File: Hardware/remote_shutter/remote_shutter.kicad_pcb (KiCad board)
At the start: 4 copper layers, 78 x 57 mm, 62 parts, among them J1 USB_C_Receptacle_USB2.0, J2 OLED, J3 AudioJack3, J4 Buzzer, J6 Switch, Q1 DMN2056U, Q2 DMN2056U, Q3 BC847BDW1, SW1 RotaryEncoder_Switch, U1 AZ1117-3.3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

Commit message: DRC error fixes.
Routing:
- net Net-(Q3-Pad5): track 0.00 -> 4.95 mm, vias 0 -> 1
- net GND: track 160.9 -> 165.3 mm, vias 26 -> 27
- net /DP: track 5.19 -> 8.74 mm, vias 0 -> 2
- net /DN: track 5.19 -> 7.92 mm
- net +3V3: track 38.0 -> 39.6 mm
- net /MCU/Interfaces/I2C.SCL: track 60.6 -> 59.9 mm

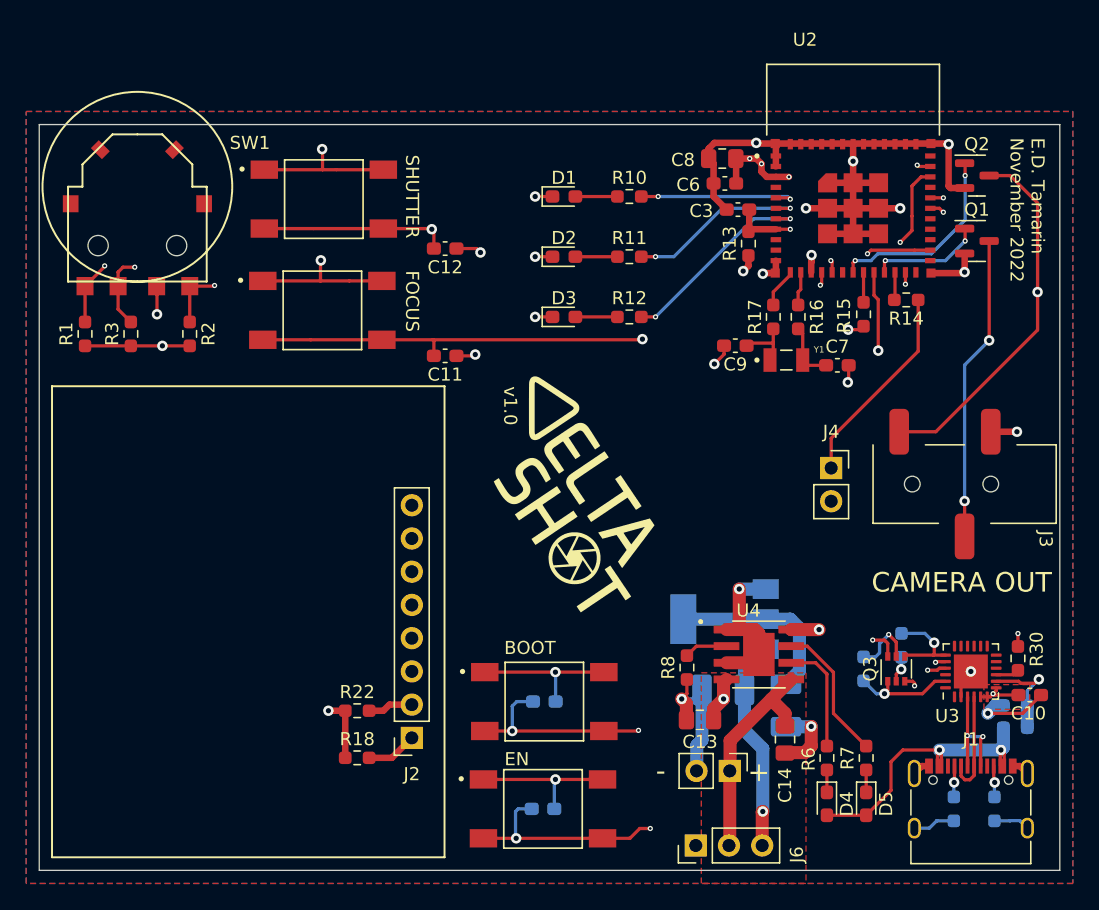
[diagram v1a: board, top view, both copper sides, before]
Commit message: Fixed via sizes. Added IO0 pullup.
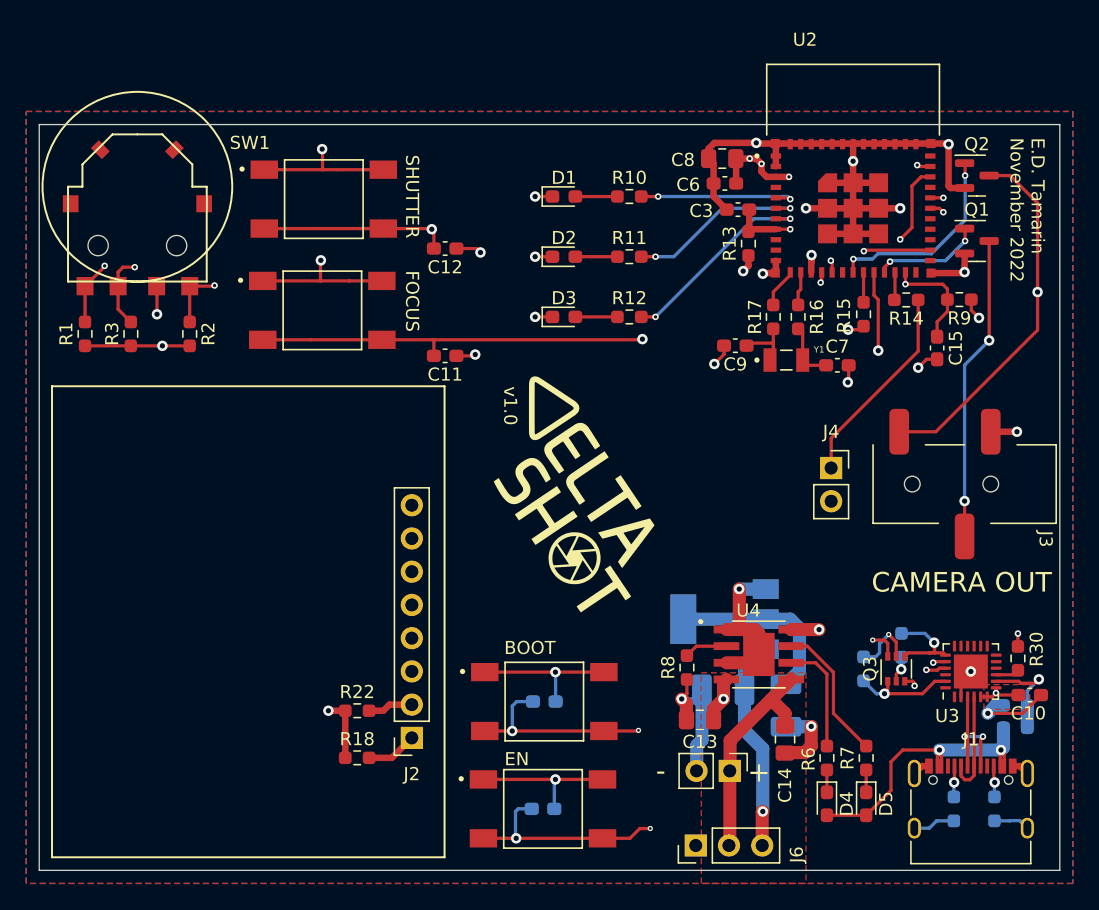
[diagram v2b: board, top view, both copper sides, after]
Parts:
- added C15: 0u1, Capacitor_SMD:C_0603_1608Metric_Pad1.08x0.95mm_HandSolder, F.Cu at (173.1, 86.1)
- added R9: 10k, Resistor_SMD:R_0603_1608Metric_Pad0.98x0.95mm_HandSolder, F.Cu at (174.8, 82.4)
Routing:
- net /MCU/IO0: track 67.9 -> 75.2 mm
- net /MCU/Interfaces/I2C.SCL: track 59.9 -> 58.0 mm
- net GND: track 165.3 -> 167.0 mm, vias 27 -> 28
- net +3V3: track 39.6 -> 41.1 mm, vias 8 -> 9

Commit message: Added debug connectors
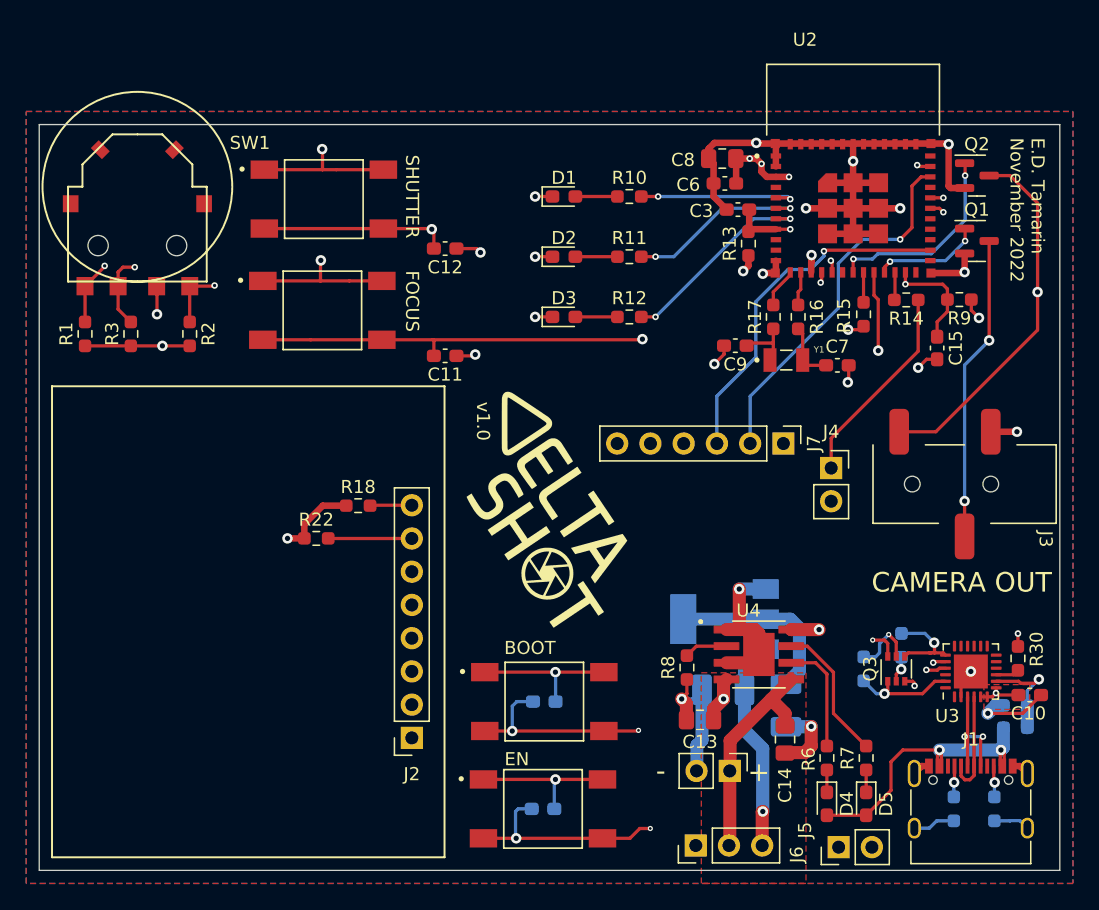
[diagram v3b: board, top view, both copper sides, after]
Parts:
- added J5: Conn_01x02_Male, Connector_PinHeader_2.54mm:PinHeader_1x02_P2.54mm_Vertical, F.Cu at (165.6, 124.2)
- added J7: Conn_01x06_Male, Connector_PinHeader_2.54mm:PinHeader_1x06_P2.54mm_Vertical, F.Cu at (161.3, 93.4)
- moved R18 19.3 mm to (128.8, 98.2)
- moved R22 13.5 mm to (125.7, 100.7)
- moved G*** 2.39 mm to (143.4, 99.2)
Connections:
- net /Comms/RX renamed /MCU/TX
- net /Comms/TX renamed /MCU/RX
- J2 pad 1: /MCU/Interfaces/I2C.SDA -> GND
- J2 pad 2: /MCU/Interfaces/I2C.SCL -> /MCU/Interfaces/5V
- J2 pad 3: /MCU/Interfaces/D/C -> +3V3
- J2 pad 4: /MCU/RST -> /MCU/Interfaces/CS
- J2 pad 5: /MCU/Interfaces/CS -> /MCU/RST
- J2 pad 6: +3V3 -> /MCU/Interfaces/D/C
- J2 pad 7: /MCU/Interfaces/5V -> /MCU/Interfaces/I2C.SCL
- J2 pad 8: GND -> /MCU/Interfaces/I2C.SDA
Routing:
- net /MCU/EN: track 93.5 -> 22.5 mm
- net /MCU/Interfaces/A2: track 61.5 -> 6.79 mm
- net /MCU/IO0: track 75.2 -> 26.0 mm
- net /MCU/Interfaces/A1: track 52.9 -> 5.47 mm
- net /MCU/RST: track 51.9 -> 7.91 mm
- net /MCU/TX: track 38.3 -> 31.2 mm
- net /MCU/RX: track 38.3 -> 33.3 mm
- net /MCU/Interfaces/I2C.SDA: track 65.4 -> 61.4 mm
- net /MCU/Interfaces/I2C.SCL: track 58.0 -> 61.8 mm
- net +3V3: track 41.1 -> 42.4 mm
- net /MCU/Interfaces/5V: track 0.00 -> 0.76 mm

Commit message: Updated routing, ground plane now empty
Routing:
- net /MCU/RST: track 7.91 -> 59.0 mm
- net /MCU/EN: track 22.5 -> 60.3 mm
- net /MCU/TX: track 31.2 -> 66.4 mm, vias 2 -> 3
- net /MCU/RX: track 33.3 -> 67.7 mm, vias 2 -> 3
- net /MCU/IO0: track 26.0 -> 54.1 mm
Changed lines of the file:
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@@
   (via (at 171.3775 111.9225) (size 0.5) (drill 0.25) (layers "F.Cu" "B.Cu") (net 3))
   (via (at 151.1775 122.8225) (size 0.4) (drill 0.2) (layers "F.Cu" "B.Cu") (net 3))
+  (segment (start 170.603235 111.9225) (end 164.730735 106.05) (width 0.25) (layer "In1.Cu") (net 3))
+  (segment (start 171.3775 111.9225) (end 170.603235 111.9225) (width 0.25) (layer "In1.Cu") (net 3))
+  (segment (start 151.1775 108.758218) (end 151.1775 122.8225) (width 0.25) (layer "In1.Cu") (net 3))
+  (segment (start 153.885718 106.05) (end 151.1775 108.758218) (width 0.25) (layer "In1.Cu") (net 3))
+  (segment (start 164.730735 106.05) (end 153.885718 106.05) (width 0.25) (layer "In1.Cu") (net 3))
   (segment (start 140.8775 123.5225) (end 140.9275 123.5725) (width 0.25) (layer "B.Cu") (net 3))
   (segment (start 140.8775 121.5225) (end 140.8775 123.5225) (width 0.25) (layer "B.Cu") (net 3))
@@
   (via (at 170.6775 81.2225) (size 0.5) (drill 0.25) (layers "F.Cu" "B.Cu") (net 4))
   (via (at 140.6275 115.3725) (size 0.8) (drill 0.4) (layers "F.Cu" "B.Cu") (net 4))
+  (segment (start 153.85 105.45) (end 150.2775 109.0225) (width 0.25) (layer "In1.Cu") (net 4))
+  (segment (start 150.2775 109.0225) (end 150.2775 115.3225) (width 0.25) (layer "In1.Cu") (net 4))
+  (segment (start 168.1775 108.4225) (end 168.1775 106.4775) (width 0.25) (layer "In1.Cu") (net 4))
+  (segment (start 167.15 105.45) (end 153.85 105.45) (width 0.25) (layer "In1.Cu") (net 4))
+  (segment (start 168.1775 106.4775) (end 167.15 105.45) (width 0.25) (layer "In1.Cu") (net 4))
   (segment (start 170.5775 83.2225) (end 170.6775 83.1225) (width 0.25) (layer "In2.Cu") (net 4))
   (segment (start 140.9775 113.1225) (end 140.6275 113.4725) (width 0.25) (layer "B.Cu") (net 4))
@@
   (segment (start 168.2775 80.3225) (end 168.2775 82.0775) (width 0.25) (layer "F.Cu") (net 11))
   (via (at 168.6 86.3) (size 0.8) (drill 0.4) (layers "F.Cu" "B.Cu") (net 11))
+  (segment (start 130.95 103.735) (end 130.95 96.7) (width 0.25) (layer "In1.Cu") (net 11))
+  (segment (start 138.202989 89.447011) (end 167.252989 89.447011) (width 0.25) (layer "In1.Cu") (net 11))
+  (segment (start 167.252989 89.447011) (end 168.6 88.1) (width 0.25) (layer "In1.Cu") (net 11))
+  (segment (start 132.9525 105.7375) (end 130.95 103.735) (width 0.25) (layer "In1.Cu") (net 11))
   (segment (start 168.6 86.3) (end 168.6 88.1) (width 0.25) (layer "In1.Cu") (net 11))
+  (segment (start 130.95 96.7) (end 138.202989 89.447011) (width 0.25) (layer "In1.Cu") (net 11))
   (segment (start 133.717482 113.3575) (end 132.9525 113.3575) (width 0.25) (layer "In2.Cu") (net 13))
   (segment (start 165.0025 92.9975) (end 165.0025 95.2725) (width 0.25) (layer "F.Cu") (net 14))
@@
   (segment (start 177.615 111.0725) (end 178.94 111.0725) (width 0.25) (layer "F.Cu") (net 33))
   (segment (start 172.296964 110.722511) (end 173.119261 110.722511) (width 0.25) (layer "F.Cu") (net 36))
+  (segment (start 151.19 86.06) (end 151.19 93.4) (width 0.25) (layer "F.Cu") (net 36))
   (segment (start 173.119261 110.722511) (end 173.269272 110.5725) (width 0.25) (layer "F.Cu") (net 36))
   (segment (start 173.2775 75.4225) (end 173.5775 75.7225) (width 0.25) (layer "F.Cu") (net 36))
   (segment (start 173.269272 110.5725) (end 173.74 110.5725) (width 0.25) (layer "F.Cu") (net 36))
+  (segment (start 156.4 80.85) (end 151.19 86.06) (width 0.25) (layer "F.Cu") (net 36))
   (segment (start 172.274453 110.7) (end 172.296964 110.722511) (width 0.25) (layer "F.Cu") (net 36))
   (segment (start 172.5775 75.4225) (end 173.2775 75.4225) (width 0.25) (layer "F.Cu") (net 36))
   (via (at 172.274453 110.7) (size 0.5) (drill 0.25) (layers "F.Cu" "B.Cu") (net 36))
+  (via (at 156.4 80.85) (size 0.8) (drill 0.4) (layers "F.Cu" "B.Cu") (net 36))
   (via (at 173.5775 75.7225) (size 0.5) (drill 0.25) (layers "F.Cu" "B.Cu") (net 36))
   (segment (start 154.35 97.85) (end 151.19 94.69) (width 0.25) (layer "In1.Cu") (net 36))
+  (segment (start 172.7 76.6) (end 164.05 76.6) (width 0.25) (layer "In1.Cu") (net 36))
+  (segment (start 157.6 79) (end 156.4 80.2) (width 0.25) (layer "In1.Cu") (net 36))
   (segment (start 162.2 97.85) (end 154.35 97.85) (width 0.25) (layer "In1.Cu") (net 36))
   (segment (start 172.274453 110.7) (end 170.098964 108.524511) (width 0.25) (layer "In1.Cu") (net 36))
+  (segment (start 173.5775 75.7225) (end 172.7 76.6) (width 0.25) (layer "In1.Cu") (net 36))
   (segment (start 151.19 94.69) (end 151.19 93.4) (width 0.25) (layer "In1.Cu") (net 36))
   (segment (start 170.098964 105.748964) (end 162.2 97.85) (width 0.25) (layer "In1.Cu") (net 36))
+  (segment (start 156.4 80.2) (end 156.4 80.85) (width 0.25) (layer "In1.Cu") (net 36))
+  (segment (start 161.65 79) (end 157.6 79) (width 0.25) (layer "In1.Cu") (net 36))
   (segment (start 170.098964 108.524511) (end 170.098964 105.748964) (width 0.25) (layer "In1.Cu") (net 36))
+  (segment (start 164.05 76.6) (end 161.65 79) (width 0.25) (layer "In1.Cu") (net 36))
   (segment (start 172.801924 110.148) (end 172.877424 110.0725) (width 0.25) (layer "F.Cu") (net 37))
+  (segment (start 153.73 85.12) (end 153.73 93.4) (width 0.25) (layer "F.Cu") (net 37))
+  (segment (start 157.55 81.098) (end 157.55 81.3) (width 0.25) (layer "F.Cu") (net 37))
   (segment (start 173.5775 74.6225) (end 172.5775 74.6225) (width 0.25) (layer "F.Cu") (net 37))
+  (segment (start 157.55 81.3) (end 153.73 85.12) (width 0.25) (layer "F.Cu") (net 37))
   (segment (start 172.877424 110.0725) (end 173.74 110.0725) (width 0.25) (layer "F.Cu") (net 37))
+  (via (at 157.55 81.098) (size 0.8) (drill 0.4) (layers "F.Cu" "B.Cu") (net 37))
   (via (at 172.801924 110.148) (size 0.5) (drill 0.25) (layers "F.Cu" "B.Cu") (net 37))
   (via (at 173.5775 74.6225) (size 0.5) (drill 0.25) (layers "F.Cu" "B.Cu") (net 37))
+  (segment (start 173.8225 74.6225) (end 173.5775 74.6225) (width 0.25) (layer "In1.Cu") (net 37))
   (segment (start 172.801924 110.148) (end 170.548484 107.89456) (width 0.25) (layer "In1.Cu") (net 37))
+  (segment (start 173.05 77.15) (end 174.3 75.9) (width 0.25) (layer "In1.Cu") (net 37))
+  (segment (start 161.977397 79.497989) (end 164.325386 77.15) (width 0.25) (layer "In1.Cu") (net 37))
   (segment (start 154.536198 97.40048) (end 153.73 96.594282) (width 0.25) (layer "In1.Cu") (net 37))
+  (segment (start 157.55 79.925386) (end 157.977397 79.497989) (width 0.25) (layer "In1.Cu") (net 37))
   (segment (start 170.548484 107.89456) (end 170.548484 105.562766) (width 0.25) (layer "In1.Cu") (net 37))
+  (segment (start 157.977397 79.497989) (end 161.977397 79.497989) (width 0.25) (layer "In1.Cu") (net 37))
   (segment (start 162.386197 97.40048) (end 154.536198 97.40048) (width 0.25) (layer "In1.Cu") (net 37))
+  (segment (start 174.3 75.9) (end 174.3 75.1) (width 0.25) (layer "In1.Cu") (net 37))
   (segment (start 153.73 96.594282) (end 153.73 93.4) (width 0.25) (layer "In1.Cu") (net 37))
+  (segment (start 157.55 81.098) (end 157.55 79.925386) (width 0.25) (layer "In1.Cu") (net 37))
+  (segment (start 164.325386 77.15) (end 173.05 77.15) (width 0.25) (layer "In1.Cu") (net 37))
+  (segment (start 174.3 75.1) (end 173.8225 74.6225) (width 0.25) (layer "In1.Cu") (net 37))
   (segment (start 170.548484 105.562766) (end 162.386197 97.40048) (width 0.25) (layer "In1.Cu") (net 37))
   (segment (start 109.4775 79.8225) (end 109.4775 79.8725) (width 0.25) (layer "F.Cu") (net 53))

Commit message: More routing updates
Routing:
- net /MCU/Interfaces/A2: track 6.79 -> 62.2 mm
- net /MCU/EN: track 60.3 -> 111.4 mm
- net /MCU/Interfaces/A1: track 5.47 -> 53.1 mm
- net /MCU/IO0: track 54.1 -> 83.9 mm
- net /MCU/Interfaces/SHUTTER: track 90.7 -> 97.6 mm

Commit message: Small updates
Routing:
- net /MCU/Interfaces/5V: track 0.76 -> 0.00 mm
- net /MCU/IO0: vias 4 -> 3
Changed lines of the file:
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@@
   (via (at 168.1775 108.4225) (size 0.4) (drill 0.2) (layers "F.Cu" "B.Cu") (net 4))
   (via (at 150.2775 115.3225) (size 0.4) (drill 0.2) (layers "F.Cu" "B.Cu") (net 4))
-  (via (at 170.6775 81.2225) (size 0.5) (drill 0.25) (layers "F.Cu" "B.Cu") (net 4))
   (via (at 140.6275 115.3725) (size 0.8) (drill 0.4) (layers "F.Cu" "B.Cu") (net 4))
   (segment (start 153.85 105.45) (end 150.2775 109.0225) (width 0.25) (layer "In1.Cu") (net 4))
@@
   (segment (start 168.6 86.3) (end 168.6 88.1) (width 0.25) (layer "In1.Cu") (net 11))
   (segment (start 130.95 96.7) (end 138.202989 89.447011) (width 0.25) (layer "In1.Cu") (net 11))
-  (segment (start 133.717482 113.3575) (end 132.9525 113.3575) (width 0.25) (layer "In2.Cu") (net 13))
   (segment (start 165.0025 92.9975) (end 165.0025 95.2725) (width 0.25) (layer "F.Cu") (net 14))
   (segment (start 171.6525 86.3475) (end 165.0025 92.9975) (width 0.25) (layer "F.Cu") (net 14))
@@
   (segment (start 125.55 82.3) (end 123.1725 79.9225) (width 0.25) (layer "In1.Cu") (net 24))
   (segment (start 159.25 82.3) (end 125.55 82.3) (width 0.25) (layer "In1.Cu") (net 24))
-  (segment (start 111.9775 79.9225) (end 111.7775 79.9225) (width 0.25) (layer "In2.Cu") (net 24))
   (segment (start 150.49 74.5225) (end 151.7775 74.5225) (width 0.25) (layer "F.Cu") (net 25))
   (segment (start 161.7775 74.6225) (end 160.7775 74.6225) (width 0.25) (layer "F.Cu") (net 25))
